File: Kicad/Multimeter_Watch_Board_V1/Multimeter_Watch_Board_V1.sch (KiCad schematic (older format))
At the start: 30 parts, among them J1 AudioJack3_Ground_renamedPins, J2 AudioJack3_Ground_renamedPins, J3 AudioJack3_Ground_renamedPins, J4 Conn_01x16_Female, J5 Conn_01x16_Female, U1 PCF85163-SO08, U2 AD8592, Y1 32kHz

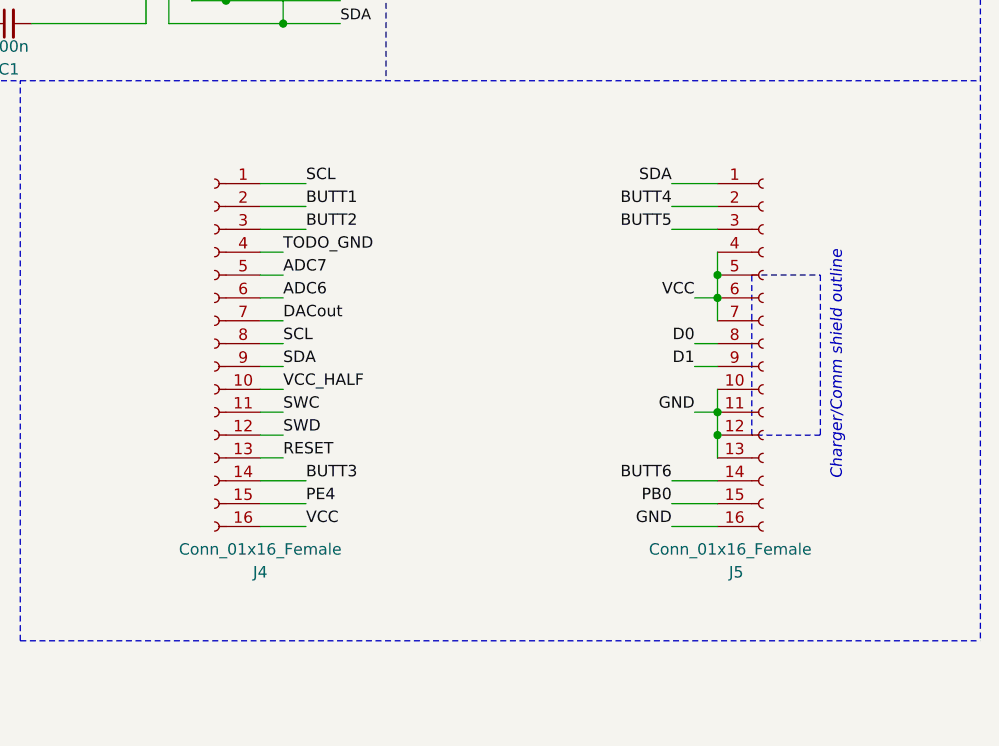
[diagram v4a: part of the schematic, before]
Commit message: Switch left and right pin headers (for simpler DACout and VCChalf routing)
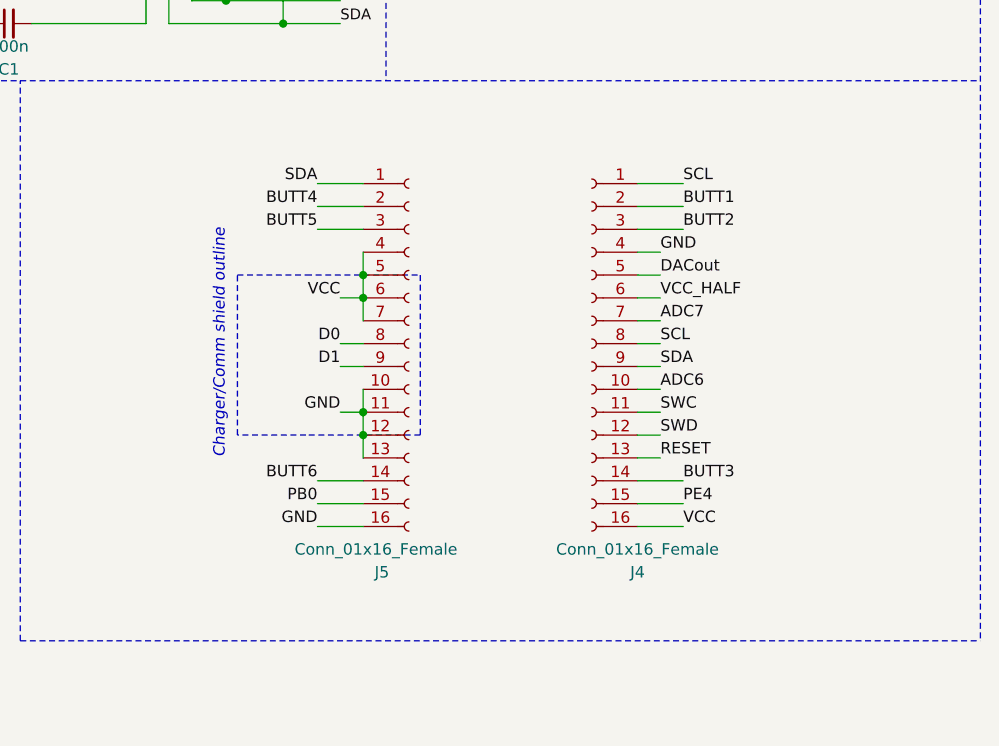
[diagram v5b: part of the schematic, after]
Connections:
- net TODO_GND is gone; now on net GND: J4.4 (Pin_4)
- net ADC1: now also J4.5 (Pin_5); no longer J4.7 (Pin_7)
- net ADC6: now also J4.10 (Pin_10); no longer J4.6 (Pin_6)
- net ADC7: now also J4.7 (Pin_7); no longer J4.5 (Pin_5)
- net VCC_HALF: now also J4.6 (Pin_6); no longer J4.10 (Pin_10)
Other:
- moved on the sheet: J4, J5
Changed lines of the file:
@@
 Wire Wire Line
 	5250 3700 5250 3800
-$Comp
-L Connector:Conn_01x16_Female J5
-U 1 1 5F44F8AA
-P 10250 5200
-F 0 "J5" H 10100 4200 50  0000 L CNN
-F 1 "Conn_01x16_Female" H 9750 4300 50  0000 L CNN
-F 2 "Connector_PinSocket_2.54mm:PinSocket_1x16_P2.54mm_Vertical" H 10250 5200 50  0001 C CNN
-F 3 "~" H 10250 5200 50  0001 C CNN
-	1    10250 5200
-	1    0    0    -1
-$EndComp
-$Comp
-L Connector:Conn_01x16_Female J4
-U 1 1 5F46892E
-P 7850 5200
-F 0 "J4" H 7650 4200 50  0000 C CNN
-F 1 "Conn_01x16_Female" H 7650 4300 50  0000 C CNN
-F 2 "Connector_PinSocket_2.54mm:PinSocket_1x16_P2.54mm_Vertical" H 7850 5200 50  0001 C CNN
-F 3 "~" H 7850 5200 50  0001 C CNN
-	1    7850 5200
-	-1   0    0    -1
-$EndComp
-Text Label 8250 4600 0    50   ~ 0
-BUTT1
-Text Label 8250 4700 0    50   ~ 0
-BUTT2
-Text Label 8250 5800 0    50   ~ 0
-BUTT3
-Text Label 9850 4600 2    50   ~ 0
-BUTT4
-Text Label 9850 4700 2    50   ~ 0
-BUTT5
-Text Label 9850 5800 2    50   ~ 0
-BUTT6
-Text Label 9850 4500 2    50   ~ 0
-SDA
-Text Label 8250 4500 0    50   ~ 0
-SCL
-Text Label 8250 5900 0    50   ~ 0
-PE4
-Wire Wire Line
-	10050 5800 9850 5800
-Wire Wire Line
-	9850 5900 10050 5900
-Wire Wire Line
-	10050 6000 9850 6000
-Wire Wire Line
-	8250 6000 8050 6000
-Wire Wire Line
-	8050 5900 8250 5900
-Wire Wire Line
-	8250 5800 8050 5800
-Wire Wire Line
-	8250 4500 8050 4500
-Wire Wire Line
-	8050 4600 8250 4600
-Wire Wire Line
-	10050 4500 9850 4500
-Wire Wire Line
-	10050 4600 9850 4600
-Text Label 9850 6000 2    50   ~ 0
-GND
-Wire Wire Line
-	10050 4700 9850 4700
-Text Label 8250 6000 0    50   ~ 0
-VCC
-Wire Wire Line
-	8050 4700 8250 4700
-Text Label 9950 5000 2    50   ~ 0
-VCC
-Text Label 9950 5500 2    50   ~ 0
-GND
-Text Label 9950 5200 2    50   ~ 0
-D0
-Text Label 9950 5300 2    50   ~ 0
-D1
-Text Label 8150 5000 0    50   ~ 0
-ADC6
-Text Label 8150 4900 0    50   ~ 0
-ADC7
-Text Label 8150 5600 0    50   ~ 0
-SWD
-Text Label 8150 5500 0    50   ~ 0
-SWC
-Text Label 8150 5100 0    50   ~ 0
-DACout
-Text Label 8150 5400 0    50   ~ 0
-VCC_HALF
-Text Label 8150 5700 0    50   ~ 0
-RESET
-Wire Wire Line
-	9950 5200 10050 5200
-Wire Wire Line
-	9950 5300 10050 5300
-Wire Wire Line
-	9950 5500 10050 5500
-Connection ~ 10050 5500
-Wire Wire Line
-	10050 5400 10050 5500
-Wire Wire Line
-	10050 5500 10050 5600
-Wire Wire Line
-	10050 5600 10050 5700
-Connection ~ 10050 5600
-Wire Wire Line
-	9950 5000 10050 5000
-Wire Wire Line
-	10050 5000 10050 5100
-Connection ~ 10050 5000
-Wire Wire Line
-	10050 5000 10050 4900
-Wire Wire Line
-	10050 4900 10050 4800
-Connection ~ 10050 4900
-Wire Wire Line
-	8150 5700 8050 5700
-Text Label 9850 5900 2    50   ~ 0
-PB0
-Wire Wire Line
-	8150 5600 8050 5600
-Wire Wire Line
-	8150 5500 8050 5500
-Wire Wire Line
-	8150 5400 8050 5400
-Wire Wire Line
-	8150 5300 8050 5300
-Wire Wire Line
-	8150 5200 8050 5200
-Wire Wire Line
-	8150 5100 8050 5100
-Wire Wire Line
-	8150 5000 8050 5000
-Wire Wire Line
-	8150 4900 8050 4900
-Wire Wire Line
-	8150 4800 8050 4800
-Text Label 8150 5300 0    50   ~ 0
-SDA
-Text Label 8150 5200 0    50   ~ 0
-SCL
-Text Label 8150 4800 0    50   ~ 0
-TODO_GND
-Wire Notes Line style dotted
-	10200 5600 10200 4900
-Wire Notes Line style dotted
-	10200 4900 10500 4900
-Wire Notes Line style dotted
-	10500 4900 10500 5600
-Wire Notes Line style dotted
-	10500 5600 10200 5600
 Text Label 3700 5000 2    50   ~ 0
 D1
@@
 Text Notes 8900 3550 0    78   Italic 0
 Has been moved to DisplayBoard
-Text Notes 10600 5800 1    50   Italic 0
-Charger/Comm shield outline
 Wire Notes Line
 	7000 6500 11200 6500
@@
 Wire Wire Line
 	10650 1150 10750 1150
+Text Label 9800 4800 0    50   ~ 0
+GND
+Text Label 9800 5200 0    50   ~ 0
+SCL
+Text Label 9800 5300 0    50   ~ 0
+SDA
+Wire Wire Line
+	9800 4800 9700 4800
+Wire Wire Line
+	9800 4900 9700 4900
+Wire Wire Line
+	9800 5000 9700 5000
+Wire Wire Line
+	9800 5100 9700 5100
+Wire Wire Line
+	9800 5200 9700 5200
+Wire Wire Line
+	9800 5300 9700 5300
+Wire Wire Line
+	9800 5400 9700 5400
+Wire Wire Line
+	9800 5500 9700 5500
+Wire Wire Line
+	9800 5600 9700 5600
+Wire Wire Line
+	9800 5700 9700 5700
+Text Label 9800 5700 0    50   ~ 0
+RESET
+Text Label 9800 5000 0    50   ~ 0
+VCC_HALF
+Text Label 9800 4900 0    50   ~ 0
+DACout
+Text Label 9800 5500 0    50   ~ 0
+SWC
+Text Label 9800 5600 0    50   ~ 0
+SWD
+Text Label 9800 5100 0    50   ~ 0
+ADC7
+Text Label 9800 5400 0    50   ~ 0
+ADC6
+Wire Wire Line
+	9700 4700 9900 4700
+Text Label 9900 6000 0    50   ~ 0
+VCC
+Wire Wire Line
+	9700 4600 9900 4600
+Wire Wire Line
+	9900 4500 9700 4500
+Wire Wire Line
+	9900 5800 9700 5800
+Wire Wire Line
+	9700 5900 9900 5900
+Wire Wire Line
+	9900 6000 9700 6000
+Text Label 9900 5900 0    50   ~ 0
+PE4
+Text Label 9900 4500 0    50   ~ 0
+SCL
+Text Label 9900 5800 0    50   ~ 0
+BUTT3
+Text Label 9900 4700 0    50   ~ 0
+BUTT2
+Text Label 9900 4600 0    50   ~ 0
+BUTT1
+$Comp
+L Connector:Conn_01x16_Female J4
+U 1 1 5F46892E
+P 9500 5200
+F 0 "J4" H 9300 4200 50  0000 C CNN
+F 1 "Conn_01x16_Female" H 9300 4300 50  0000 C CNN
+F 2 "Connector_PinSocket_2.54mm:PinSocket_1x16_P2.54mm_Vertical" H 9500 5200 50  0001 C CNN
+F 3 "~" H 9500 5200 50  0001 C CNN
+	1    9500 5200
+	-1   0    0    -1
+$EndComp
+Text Notes 7900 4700 3    50   Italic 0
+Charger/Comm shield outline
+Wire Notes Line style dotted
+	7950 4900 8250 4900
+Wire Notes Line style dotted
+	7950 5600 7950 4900
+Wire Notes Line style dotted
+	8250 5600 7950 5600
+Text Label 8300 5900 2    50   ~ 0
+PB0
+Connection ~ 8500 4900
+Wire Wire Line
+	8500 4900 8500 4800
+Wire Wire Line
+	8500 5000 8500 4900
+Connection ~ 8500 5000
+Wire Wire Line
+	8500 5000 8500 5100
+Wire Wire Line
+	8400 5000 8500 5000
+Connection ~ 8500 5600
+Wire Wire Line
+	8500 5600 8500 5700
+Wire Wire Line
+	8500 5500 8500 5600
+Wire Wire Line
+	8500 5400 8500 5500
+Connection ~ 8500 5500
+Wire Wire Line
+	8400 5500 8500 5500
+Wire Wire Line
+	8400 5300 8500 5300
+Wire Wire Line
+	8400 5200 8500 5200
+Text Label 8400 5300 2    50   ~ 0
+D1
+Text Label 8400 5200 2    50   ~ 0
+D0
+Text Label 8400 5500 2    50   ~ 0
+GND
+Text Label 8400 5000 2    50   ~ 0
+VCC
+Wire Wire Line
+	8500 4700 8300 4700
+Text Label 8300 6000 2    50   ~ 0
+GND
+Wire Wire Line
+	8500 4600 8300 4600
+Wire Wire Line
+	8500 4500 8300 4500
+Wire Wire Line
+	8500 6000 8300 6000
+Wire Wire Line
+	8300 5900 8500 5900
+Wire Wire Line
+	8500 5800 8300 5800
+Text Label 8300 4500 2    50   ~ 0
+SDA
+Text Label 8300 5800 2    50   ~ 0
+BUTT6
+Text Label 8300 4700 2    50   ~ 0
+BUTT5
+Text Label 8300 4600 2    50   ~ 0
+BUTT4
+$Comp
+L Connector:Conn_01x16_Female J5
+U 1 1 5F44F8AA
+P 8700 5200
+F 0 "J5" H 8550 4200 50  0000 L CNN
+F 1 "Conn_01x16_Female" H 8200 4300 50  0000 L CNN
+F 2 "Connector_PinSocket_2.54mm:PinSocket_1x16_P2.54mm_Vertical" H 8700 5200 50  0001 C CNN
+F 3 "~" H 8700 5200 50  0001 C CNN
+	1    8700 5200
+	1    0    0    -1
+$EndComp
+Wire Notes Line
+	8250 4900 8750 4900
+Wire Notes Line
+	8750 4900 8750 5600
+Wire Notes Line
+	8750 5600 8250 5600
 $EndSCHEMATC

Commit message: first attempt at processor board layout
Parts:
- U1: footprint Package_SO:SOIC-8-1EP_3.9x4.9mm_P1.27mm_EP2.29x3mm -> Package_SO:SOIC-8-N7_3.9x4.9mm_P1.27mm
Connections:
- net AD10 is gone; now on net ADC10: CPU1.20 (PE6)
- net AD11 is gone; now on net ADC11: CPU1.17 (PB5)
- net ADC1: now also J4.6 (Pin_6); no longer J4.5 (Pin_5)
- net ADC10: now also R1.2, R2.1
- net ADC2: now also J2.2; no longer F1.2
- net ADC3: now also F1.2; no longer J2.3
- net ADC6: now also J4.8 (Pin_8); no longer J4.10 (Pin_10)
- net ADC7: now also J4.9 (Pin_9); no longer J4.7 (Pin_7)
- net BUTT1: now also J4.3 (Pin_3); no longer J4.2 (Pin_2)
- net BUTT2: now also J4.2 (Pin_2); no longer J4.3 (Pin_3)
- net GND: now also J5.1 (Pin_1); no longer J5.16 (Pin_16)
- net PE4: now also J5.16 (Pin_16); no longer J4.15 (Pin_15)
- net RESET: now also J4.7 (Pin_7); no longer J4.13 (Pin_13)
- net SCL: now also J4.11 (Pin_11), J4.16 (Pin_16); no longer J4.1 (Pin_1), J4.8 (Pin_8)
- net SDA: now also J4.10 (Pin_10), J4.15 (Pin_15); no longer J4.9 (Pin_9), J5.1 (Pin_1)
- net SWC: now also J4.13 (Pin_13); no longer J4.11 (Pin_11)
- net VCC: now also J4.1 (Pin_1); no longer J4.16 (Pin_16)
- net VCC_HALF: now also J4.5 (Pin_5); no longer J4.6 (Pin_6)
- net at F1.1: now also J2.3; no longer J2.2
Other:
- moved on the sheet: F1, R6
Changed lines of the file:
@@
 Text Label 6750 1400 0    47   ~ 0
 ADC11
-Text Label 7150 2100 1    47   ~ 0
+Text Label 7050 2100 1    47   ~ 0
 ADC2
-Text Label 7550 2100 1    47   ~ 0
+Text Label 7450 2100 1    47   ~ 0
 ADC3
 Text Notes 5150 1700 0    118  ~ 0
@@
 $EndComp
 Wire Wire Line
-	7150 2200 7150 2300
+	7050 2200 7050 2300
 $Comp
 L Multimeter_Watch_Custom_Symbols:AudioJack3_Ground_renamedPins J3
@@
 F 0 "U1" H 7000 3809 47  0000 C CNN
 F 1 "PCF85163-SO08" H 7000 3722 47  0000 C CNN
-F 2 "Package_SO:SOIC-8-1EP_3.9x4.9mm_P1.27mm_EP2.29x3mm" H 6900 3400 47  0001 C CNN
+F 2 "Package_SO:SOIC-8-N7_3.9x4.9mm_P1.27mm" H 6900 3400 47  0001 C CNN
 F 3 "" H 6900 3400 47  0001 C CNN
 	1    7000 3450
@@
 L Device:R R6
 U 1 1 5F2246FE
-P 7350 2200
-F 0 "R6" V 7150 2200 50  0000 C CNN
-F 1 "R_shunt" V 7250 2200 50  0000 C CNN
-F 2 "Resistor_SMD:R_2512_6332Metric_Pad1.52x3.35mm_HandSolder" V 7280 2200 50  0001 C CNN
-F 3 "~" H 7350 2200 50  0001 C CNN
-	1    7350 2200
+P 7250 2200
+F 0 "R6" V 7050 2200 50  0000 C CNN
+F 1 "R_shunt" V 7150 2200 50  0000 C CNN
+F 2 "Resistor_SMD:R_2512_6332Metric_Pad1.52x3.35mm_HandSolder" V 7180 2200 50  0001 C CNN
+F 3 "~" H 7250 2200 50  0001 C CNN
+	1    7250 2200
 	0    1    1    0
 $EndComp
 Wire Wire Line
-	7200 2200 7150 2200
-Wire Wire Line
-	7500 2200 7550 2200
-Wire Wire Line
-	7550 2200 7550 2100
-Connection ~ 7550 2200
-Wire Wire Line
-	7550 2200 7800 2200
-Wire Wire Line
-	7150 2200 7150 2100
-Connection ~ 7150 2200
+	7100 2200 7050 2200
+Wire Wire Line
+	7050 2200 7050 2100
+Connection ~ 7050 2200
 Wire Wire Line
 	6550 3300 6450 3300
@@
 Wire Wire Line
 	6150 3400 6550 3400
-Text Label 5300 1400 0    47   ~ 0
+Text Label 5550 1400 0    47   ~ 0
 ADC10
 Wire Wire Line
@@
 L Device:Fuse F1
 U 1 1 5F402451
-P 7650 2300
-F 0 "F1" V 7750 2300 50  0000 C CNN
-F 1 "Fuse" V 7800 2300 50  0000 C CNN
-F 2 "Fuse:Fuse_0805_2012Metric_Pad1.15x1.40mm_HandSolder" V 7580 2300 50  0001 C CNN
-F 3 "~" H 7650 2300 50  0001 C CNN
-	1    7650 2300
+P 7650 2200
+F 0 "F1" V 7750 2200 50  0000 C CNN
+F 1 "Fuse" V 7800 2200 50  0000 C CNN
+F 2 "Fuse:Fuse_0805_2012Metric_Pad1.15x1.40mm_HandSolder" V 7580 2200 50  0001 C CNN
+F 3 "~" H 7650 2200 50  0001 C CNN
+	1    7650 2200
 	0    1    1    0
 $EndComp
-Wire Wire Line
-	7500 2300 7150 2300
 $Comp
 L Device:Battery_Cell BT1
@@
 ADC0
 Text Label 4950 6250 0    50   ~ 0
-AD11
+ADC11
 Text Label 4950 5950 0    50   ~ 0
-AD10
+ADC10
 Text Label 4950 5750 0    50   ~ 0
 ADC7
@@
 Text Label 9800 4800 0    50   ~ 0
 GND
-Text Label 9800 5200 0    50   ~ 0
+Text Label 9800 5500 0    50   ~ 0
 SCL
-Text Label 9800 5300 0    50   ~ 0
+Text Label 9800 5400 0    50   ~ 0
 SDA
 Wire Wire Line
@@
 Wire Wire Line
 	9800 5700 9700 5700
+Text Label 9800 5100 0    50   ~ 0
+RESET
+Text Label 9800 4900 0    50   ~ 0
+VCC_HALF
+Text Label 9800 5000 0    50   ~ 0
+DACout
 Text Label 9800 5700 0    50   ~ 0
-RESET
-Text Label 9800 5000 0    50   ~ 0
-VCC_HALF
-Text Label 9800 4900 0    50   ~ 0
-DACout
-Text Label 9800 5500 0    50   ~ 0
 SWC
 Text Label 9800 5600 0    50   ~ 0
 SWD
-Text Label 9800 5100 0    50   ~ 0
+Text Label 9800 5300 0    50   ~ 0
 ADC7
-Text Label 9800 5400 0    50   ~ 0
+Text Label 9800 5200 0    50   ~ 0
 ADC6
 Wire Wire Line
 	9700 4700 9900 4700
+Wire Wire Line
+	9700 4600 9900 4600
+Wire Wire Line
+	9900 4500 9700 4500
+Wire Wire Line
+	9900 5800 9700 5800
+Wire Wire Line
+	9700 5900 9900 5900
+Wire Wire Line
+	9900 6000 9700 6000
 Text Label 9900 6000 0    50   ~ 0
-VCC
-Wire Wire Line
-	9700 4600 9900 4600
-Wire Wire Line
-	9900 4500 9700 4500
-Wire Wire Line
-	9900 5800 9700 5800
-Wire Wire Line
-	9700 5900 9900 5900
-Wire Wire Line
-	9900 6000 9700 6000
-Text Label 9900 5900 0    50   ~ 0
-PE4
-Text Label 9900 4500 0    50   ~ 0
 SCL
 Text Label 9900 5800 0    50   ~ 0
 BUTT3
+Text Label 9900 4600 0    50   ~ 0
+BUTT2
 Text Label 9900 4700 0    50   ~ 0
-BUTT2
-Text Label 9900 4600 0    50   ~ 0
 BUTT1
 $Comp
@@
 Wire Notes Line style dotted
 	8250 5600 7950 5600
-Text Label 8300 5900 2    50   ~ 0
-PB0
 Connection ~ 8500 4900
 Wire Wire Line
@@
 Wire Wire Line
 	8500 4700 8300 4700
-Text Label 8300 6000 2    50   ~ 0
-GND
 Wire Wire Line
 	8500 4600 8300 4600
@@
 Wire Wire Line
 	8500 5800 8300 5800
-Text Label 8300 4500 2    50   ~ 0
+Text Label 9900 5900 0    50   ~ 0
 SDA
 Text Label 8300 5800 2    50   ~ 0
@@
 Wire Notes Line
 	8750 5600 8250 5600
+Wire Wire Line
+	7500 2200 7450 2200
+Wire Wire Line
+	7450 2200 7450 2100
+Connection ~ 7450 2200
+Wire Wire Line
+	7450 2200 7400 2200
+Wire Wire Line
+	7050 2300 7800 2300
+Text Label 9900 4500 0    50   ~ 0
+VCC
+Text Label 8300 6000 2    50   ~ 0
+PE4
+Text Label 8300 4500 2    50   ~ 0
+GND
+Text Label 8300 5900 2    50   ~ 0
+PB0
 $EndSCHEMATC
